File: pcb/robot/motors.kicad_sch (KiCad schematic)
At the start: 46 parts, among them J5 MotorCable, J6 Conn_01x06_MountingPin, J7 Conn_01x06_MountingPin, J8 MotorCable, Q6 SN74AHC125RGYR, Q7 AO3400A, U25 DRV8830DRCR, U26 DRV8830DRCR, U32 MCP6541T-I/OT, U33 MAX6006AEUR+T

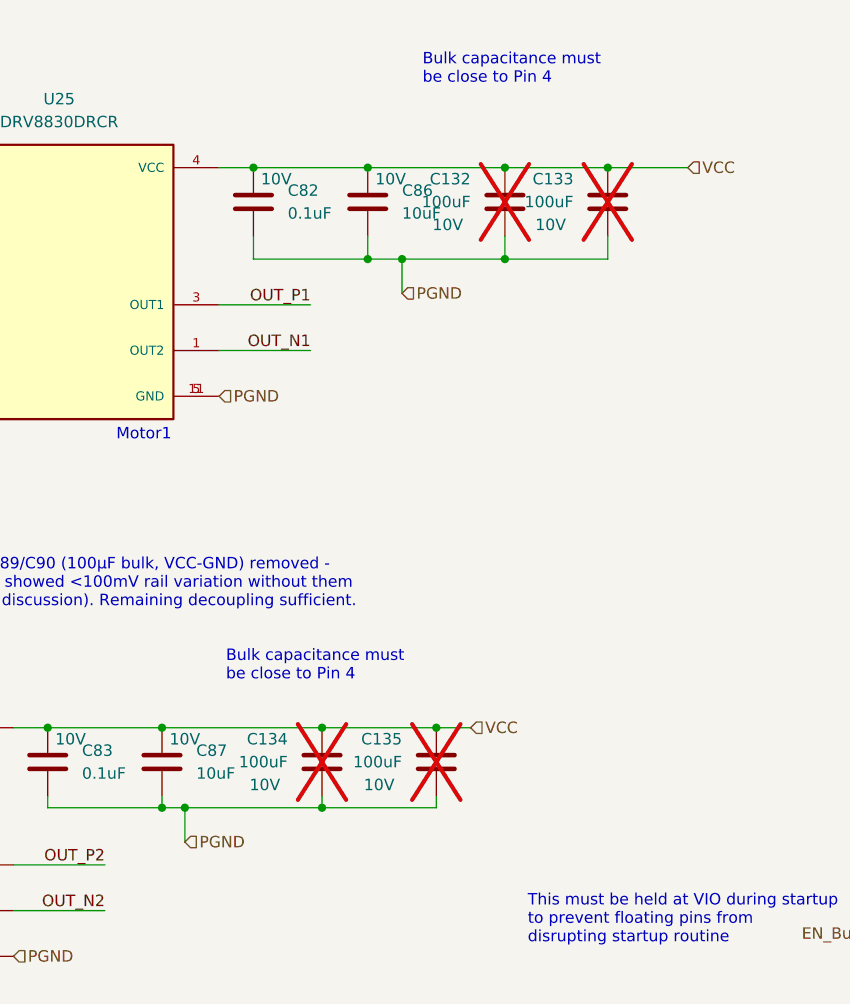
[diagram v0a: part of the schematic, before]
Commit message: Populate 2 of 4 motor-VCC bulk caps with real 100uF/16V parts (#25)
C132 and C134 (nearest each DRV8830) now use the real
APXK160ARA101MF611 (NCC, 100uF/16V/24mOhm ESR/2.49A ripple) instead
of a mismatched BOM entry that pointed to an unrelated 1206 ceramic
part. C133/C135 stay DNP for bring-up tuning, same part assigned to
keep BOM data consistent across all four positions.

Verified via kicad-cli: ERC +4 (cosmetic lib-symbol-mismatch warnings,
same class as the pre-existing U12 issue), DRC 0 unconnected, same
single pre-existing parity warning, net -7 DRC warnings overall.
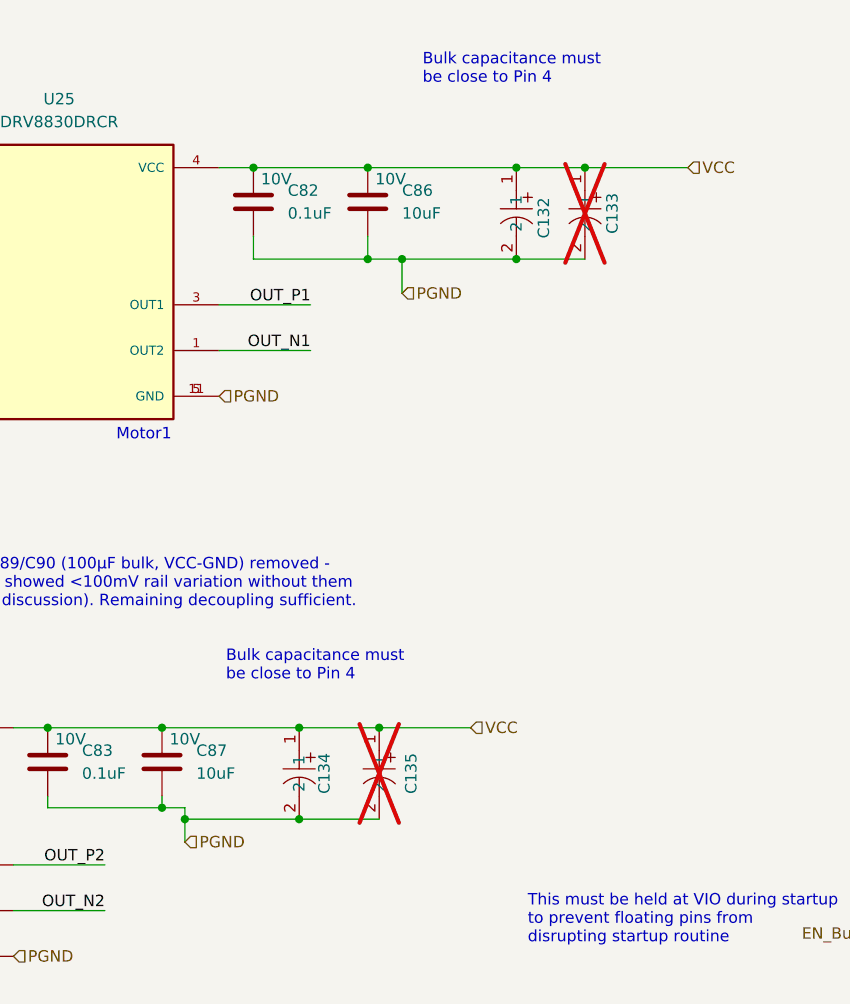
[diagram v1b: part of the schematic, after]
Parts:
- removed C132, C133, C134, C135: 100uF, robot:CP_Elec_APXJ100ARA271MF61G, symbol robot:C
- added C132, C133, C134, C135: APXK160ARA101MF611, easyeda2kicad:CAP-SMD_BD6.3-L6.6-W6.6-FD, symbol easyeda2kicad:APXK160ARA101MF611
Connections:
- net PGND: now also C132.2, C133.2, C134.2, C135.2
- net VCC: now also C132.1, C133.1, C134.1, C135.1

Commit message: Gate MAX77857 EN via GPIO22 divider, bump C136 to 100nF (#24)
R135/R136 (10k/10k) now gate U23.EN from GPIO22 instead of tying it
straight to 1.8V. GPIO22 low or floating (RP2040 reset/boot default)
holds EN at 0V, no firmware dependency for the off-state. VIO stays
on 1.8V, untouched. C136 220pF -> 100nF (CL05A104KA5NNNC) to meet
the MAX6006's real >=10nF minimum.

Verified against baseline: ERC 337/337 (no new violations), DRC 0
unconnected items, no violations tied to the new parts.
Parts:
- removed C136: 220pF, easyeda2kicad:C0402, symbol easyeda2kicad:CC0402FRNPO9BN221
- added C136: 0.1uF, robot:C_0402_1005Metric, symbol robot:C
- C132, C133: Part Number (none) -> APXK160ARA101MF611
- C134, C135: MPN APXK160ARA101MF611 -> (none); Part Number (none) -> APXK160ARA101MF611
- Q7: MPN AO3400A -> (none); Part Number (none) -> AO3400A
- R124, R126, R127: MPN FRC2512F2R70TS -> (none); Part Number (none) -> FRC2512F2R70TS
- R128: MPN 0603WAF3483T5E -> (none); Part Number (none) -> 0603WAF3483T5E
- R129, R132: MPN 0603WAF1003T5E -> (none); Part Number (none) -> 0603WAF1003T5E
- R130: MPN 0603WAF5904T5E -> (none); Part Number (none) -> 0603WAF5904T5E
- R131: MPN 0402WGF4123TCE -> (none); Part Number (none) -> 0402WGF4123TCE
- U32: MPN MCP6541T-I/OT -> (none); Part Number (none) -> MCP6541T-I/OT
- U33: MPN MAX6006AEUR+T -> (none); Part Number (none) -> MAX6006AEUR+T
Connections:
- net PGND: now also C136.1
- net at R131.1, U32.4 (VIN-), U33.1 (OUT): now also C136.2
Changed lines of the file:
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@@
 	)
 	(junction
+		(at 119.38 198.12)
+		(diameter 0)
+		(color 0 0 0 0)
+	)
+	(junction
 		(at 121.92 102.87)
 		(diameter 0)
@@
 	)
 	(junction
-		(at 119.38 198.12)
-		(diameter 0)
-		(color 0 0 0 0)
-	)
-	(junction
 		(at 68.58 185.42)
 		(diameter 0)
@@
 	(wire
 		(pts
-			(xy 119.38 198.12) (xy 121.92 198.12)
-		)
-		(stroke
-			(width 0)
-			(type default)
-		)
-	)
-	(wire
-		(pts
 			(xy 101.6 170.18) (xy 80.01 170.18)
 		)
@@
 	(wire
 		(pts
+			(xy 119.38 195.58) (xy 119.38 198.12)
+		)
+		(stroke
+			(width 0)
+			(type default)
+		)
+	)
+	(wire
+		(pts
 			(xy 73.66 160.02) (xy 74.93 160.02)
 		)
@@
 	(wire
 		(pts
+			(xy 119.38 198.12) (xy 121.92 198.12)
+		)
+		(stroke
+			(width 0)
+			(type default)
+		)
+	)
+	(wire
+		(pts
 			(xy 146.05 30.48) (xy 153.67 30.48)
 		)
@@
 			)
 		)
+		(property "Part Number" "APXK160ARA101MF611"
+			(at 146.05 35.56 0)
+			(effects
+				(font
+					(size 1.27 1.27)
+				)
+				(hide yes)
+			)
+		)
 		(pin "2"
 		)
@@
 			)
 		)
-		(property "MPN" "FRC2512F2R70TS"
+		(property "Part Number" "FRC2512F2R70TS"
 			(at 68.58 168.91 0)
 			(effects
@@
 			)
 		)
+		(property "Part Number" "APXK160ARA101MF611"
+			(at 153.67 35.56 0)
+			(effects
+				(font
+					(size 1.27 1.27)
+				)
+				(hide yes)
+			)
+		)
 		(pin "2"
 		)
@@
 	)
 	(symbol
-		(lib_id "easyeda2kicad:CC0402FRNPO9BN221")
-		(at 119.38 193.04 270)
-		(unit 1)
-		(exclude_from_sim no)
-		(in_bom yes)
-		(on_board yes)
-		(dnp no)
-		(property "Reference" "C136"
-			(at 123.19 193.04 0)
-			(effects
-				(font
-					(size 1.27 1.27)
-				)
-			)
-		)
-		(property "Value" "220pF"
-			(at 115.824 193.294 0)
-			(effects
-				(font
-					(size 1.27 1.27)
-				)
-			)
-		)
-		(property "Footprint" "easyeda2kicad:C0402"
-			(at 111.76 193.04 0)
-			(effects
-				(font
-					(size 1.27 1.27)
-				)
-				(hide yes)
-			)
-		)
-		(property "Datasheet" "https://lcsc.com/product-detail/Multilayer-Ceramic-Capacitors-MLCC-SMD-SMT_YAGEO-CC0402FRNPO9BN221_C326765.html"
-			(at 109.22 193.04 0)
-			(effects
-				(font
-					(size 1.27 1.27)
-				)
-				(hide yes)
-			)
-		)
-		(property "Description" "CC0402FRNPO9BN221"
-			(at 119.38 193.04 0)
-			(effects
-				(font
-					(size 1.27 1.27)
-				)
-				(hide yes)
-			)
-		)
-		(property "Manufacturer" "YAGEO(国巨)"
-			(at 106.68 193.04 0)
-			(effects
-				(font
-					(size 1.27 1.27)
-				)
-				(hide yes)
-			)
-		)
-		(property "MPN" "CC0402FRNPO9BN221"
-			(at 104.14 193.04 0)
-			(effects
-				(font
-					(size 1.27 1.27)
-				)
-				(hide yes)
-			)
-		)
-		(property "LCSC Part" "C326765"
-			(at 101.6 193.04 0)
-			(effects
-				(font
-					(size 1.27 1.27)
-				)
-				(hide yes)
-			)
-		)
-		(pin "1"
-		)
-		(pin "2"
-		)
-		(instances
-			(project ""
-				(path "/0c7b298e-2d07-4b1f-b033-e95f02d45089/4bf796fd-fdb4-45d1-808a-a634d5f4571e"
-					(reference "C136")
-					(unit 1)
-				)
-			)
-		)
-	)
-	(symbol
 		(lib_id "robot:Conn_01x06_MountingPin")
 		(at 232.41 52.07 0)
@@
 			)
 		)
-		(property "MPN" "0402WGF4123TCE"
+		(property "Part Number" "0402WGF4123TCE"
 			(at 137.16 177.8 0)
 			(effects
@@
 			)
 		)
-		(property "MPN" "FRC2512F2R70TS"
+		(property "Part Number" "FRC2512F2R70TS"
 			(at 68.58 162.56 0)
 			(effects
@@
 	(symbol
 		(lib_id "robot:C")
+		(at 119.38 191.77 180)
+		(unit 1)
+		(exclude_from_sim no)
+		(in_bom yes)
+		(on_board yes)
+		(dnp no)
+		(property "Reference" "C136"
+			(at 115.57 193.0401 0)
+			(effects
+				(font
+					(size 1.27 1.27)
+				)
+				(justify left)
+			)
+		)
+		(property "Value" "0.1uF"
+			(at 115.57 190.5001 0)
+			(effects
+				(font
+					(size 1.27 1.27)
+				)
+				(justify left)
+			)
+		)
+		(property "Footprint" "robot:C_0402_1005Metric"
+			(at 118.4148 187.96 0)
+			(effects
+				(font
+					(size 1.27 1.27)
+				)
+				(hide yes)
+			)
+		)
+		(property "Datasheet" "~"
+			(at 119.38 191.77 0)
+			(effects
+				(font
+					(size 1.27 1.27)
+				)
+				(hide yes)
+			)
+		)
+		(property "Description" "10V"
+			(at 116.84 194.31 0)
+			(effects
+				(font
+					(size 1.27 1.27)
+				)
+			)
+		)
+		(property "Manufacturer" "Samsung"
+			(at 119.38 191.77 0)
+			(effects
+				(font
+					(size 1.27 1.27)
+				)
+				(hide yes)
+			)
+		)
+		(property "Part Number" "CL05A104KA5NNNC"
+			(at 119.38 191.77 0)
+			(effects
+				(font
+					(size 1.27 1.27)
+				)
+				(hide yes)
+			)
+		)
+		(property "Stock" ""
+			(at 119.38 191.77 0)
+			(effects
+				(font
+					(size 1.27 1.27)
+				)
+				(hide yes)
+			)
+		)
+		(property "Type" "SMD"
+			(at 119.38 191.77 0)
+			(effects
+				(font
+					(size 1.27 1.27)
+				)
+				(hide yes)
+			)
+		)
+		(pin "1"
+		)
+		(pin "2"
+		)
+		(instances
+			(project "robot"
+				(path "/0c7b298e-2d07-4b1f-b033-e95f02d45089/4bf796fd-fdb4-45d1-808a-a634d5f4571e"
+					(reference "C136")
+					(unit 1)
+				)
+			)
+		)
+	)
+	(symbol
+		(lib_id "robot:C")
 		(at 116.84 34.29 0)
 		(unit 1)
@@
 			)
 		)
-		(property "MPN" "0603WAF1003T5E"
+		(property "Part Number" "0603WAF1003T5E"
 			(at 44.45 191.77 0)
 			(effects
@@
 			)
 		)
-		(property "MPN" "0603WAF5904T5E"
+		(property "Part Number" "0603WAF5904T5E"
 			(at 83.82 180.34 0)
 			(effects
@@
 			)
 		)
-		(property "MPN" "MCP6541T-I/OT"
+		(property "Part Number" "MCP6541T-I/OT"
 			(at 92.71 200.66 0)
 			(effects
@@
 			)
 		)
-		(property "MPN" "MAX6006AEUR+T"
+		(property "Part Number" "MAX6006AEUR+T"
 			(at 132.08 209.55 0)
 			(effects
@@
 			)
 		)
-		(property "MPN" "AO3400A"
+		(property "Part Number" "AO3400A"
 			(at 100.33 162.56 0)
 			(effects
@@
 			)
 		)
-		(property "MPN" "APXK160ARA101MF611"
+		(property "Part Number" "APXK160ARA101MF611"
 			(at 115.57 97.79 0)
 			(effects
@@
 			)
 		)
-		(property "MPN" "0603WAF1003T5E"
+		(property "Part Number" "0603WAF1003T5E"
 			(at 87.63 181.61 0)
 			(effects
@@
 			)
 		)
-		(property "MPN" "APXK160ARA101MF611"
+		(property "Part Number" "APXK160ARA101MF611"
 			(at 106.68 97.79 0)
 			(effects
@@
 			)
 		)
-		(property "MPN" "0603WAF3483T5E"
+		(property "Part Number" "0603WAF3483T5E"
 			(at 44.45 177.8 0)
 			(effects
@@
 			)
 		)
-		(property "MPN" "FRC2512F2R70TS"
+		(property "Part Number" "FRC2512F2R70TS"
 			(at 68.58 175.26 0)
 			(effects
